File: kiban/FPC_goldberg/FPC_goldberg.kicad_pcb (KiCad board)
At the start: 2 copper layers, 68.5 x 87.4 mm, 162 parts, among them J1 IN, J2 OUT

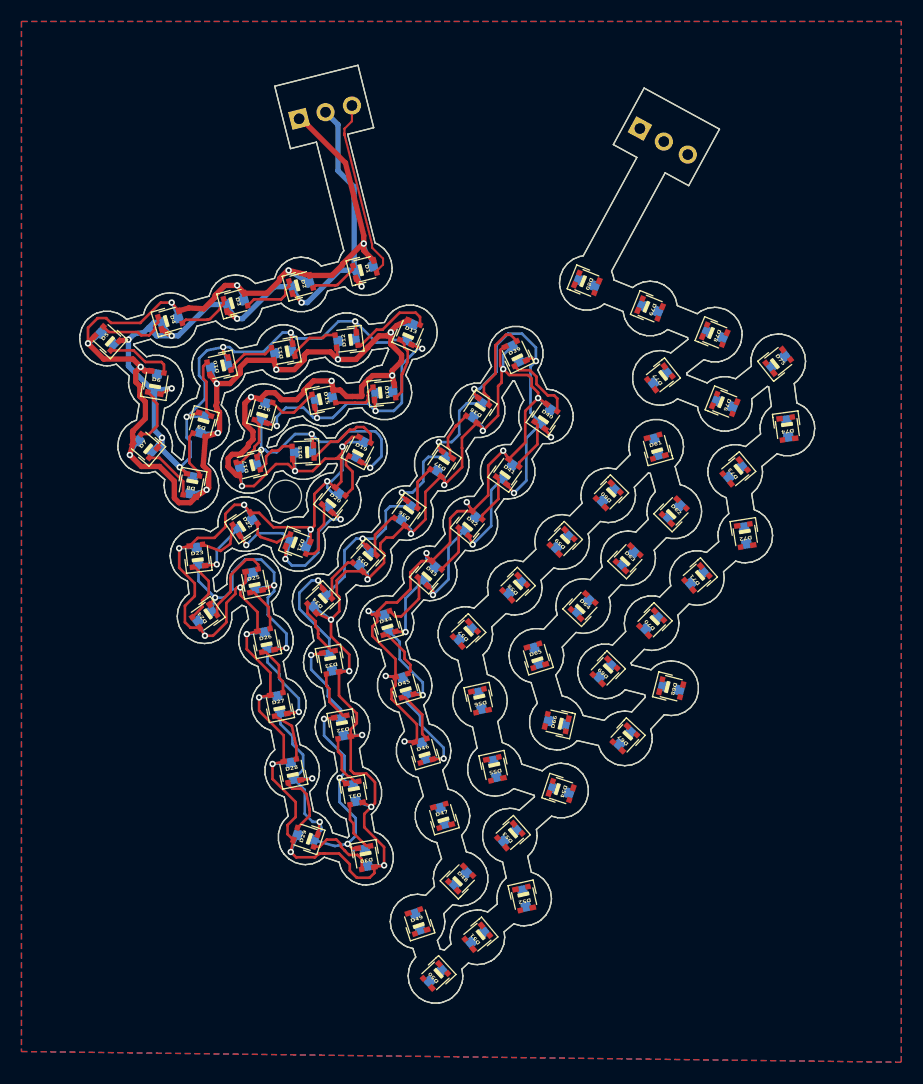
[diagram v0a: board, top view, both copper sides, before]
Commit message: kiban: regenerate FPC_goldberg fabrication outputs
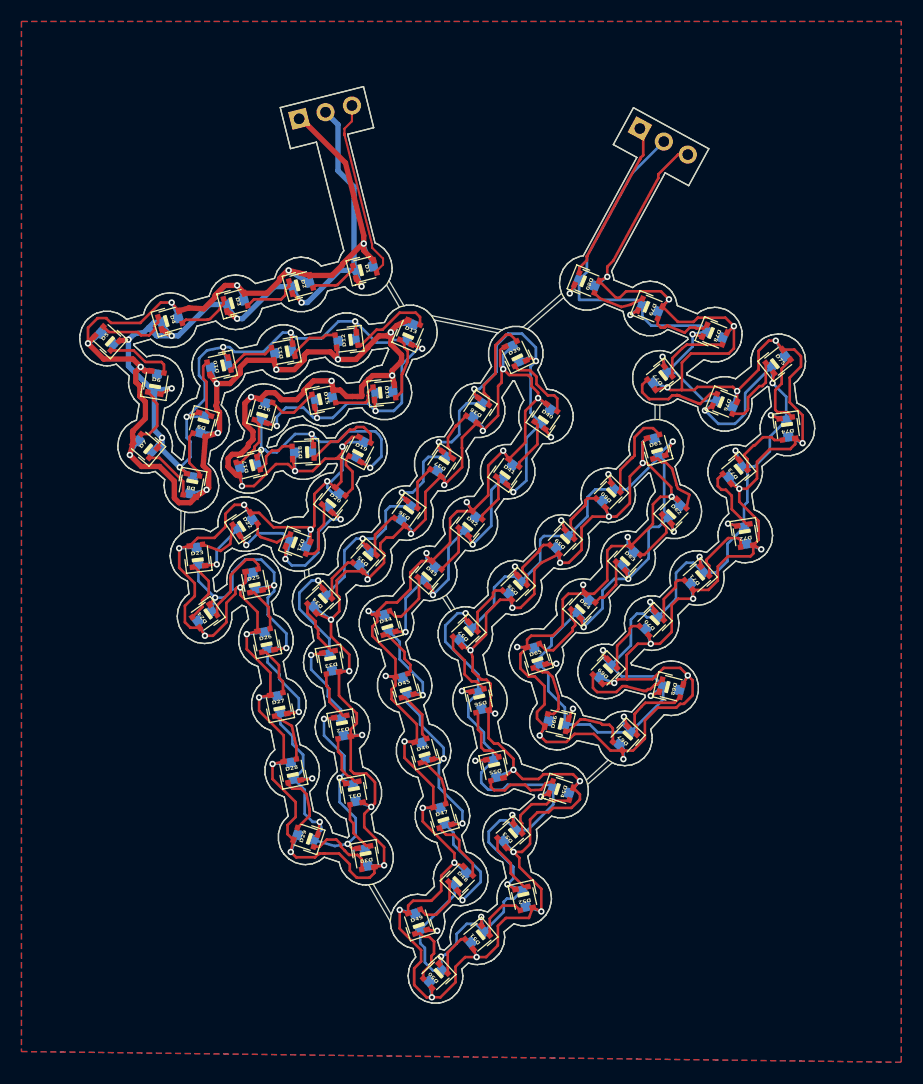
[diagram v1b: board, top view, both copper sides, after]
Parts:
- turned C47 to -73.848 degrees
- turned C48 to -135.007 degrees
- turned C49 to -71.809 degrees
- turned C50 to 42.69 degrees
- turned C51 to 39.664 degrees
- turned C52 to 102.838 degrees
- turned C53 to 41.324 degrees
- turned C54 to 161.833 degrees
- turned C55 to 102.357 degrees
- turned C56 to 102.371 degrees
- turned C57 to 43.148 degrees
- turned C58 to 44.086 degrees
- turned C59 to 45.306 degrees
- turned C60 to 45.315 degrees
- turned C61 to -74.437 degrees
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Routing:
- net +5V: track 456.1 -> 819.3 mm, vias 46 -> 80
- net GND: track 429.6 -> 765.6 mm, vias 46 -> 80
- net DOUT: track 0.00 -> 15.3 mm
- net Net-(D76-DOUT): track 0.00 -> 9.37 mm
- net Net-(D68-DOUT): track 0.00 -> 8.63 mm
- net Net-(D60-DOUT): track 0.00 -> 8.61 mm
- net Net-(D54-DOUT): track 0.00 -> 7.26 mm
- net Net-(D74-DOUT): track 0.00 -> 7.14 mm
- net Net-(D67-DOUT): track 0.00 -> 6.93 mm
- net Net-(D53-DOUT): track 0.00 -> 6.89 mm
- net Net-(D77-DOUT): track 0.00 -> 6.84 mm
- net Net-(D75-DOUT): track 0.00 -> 6.81 mm
- net Net-(D61-DOUT): track 0.00 -> 6.61 mm
- net OUT9: track 0.00 -> 6.53 mm
- net Net-(D66-DOUT): track 0.00 -> 6.35 mm
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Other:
- board size 68.5 x 87.4 mm -> 68.5 x 85.4 mm
